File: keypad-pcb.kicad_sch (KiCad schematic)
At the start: 34 parts, among them J1 AVR-ISP-6, SW0 SW_Push, SW1 SW_Push, SW2 SW_Push, SW3 SW_Push, SW4 SW_Push, SW5 SW_Push, SW6 SW_Push, U1 ATmega32U4-A, Y1 Crystal_GND24_Small

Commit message: arrange parts
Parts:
- removed R5, R6: 22, Resistor_SMD:R_0805_2012Metric, symbol Device:R_Small
- F1: value Polyfuse_Small -> 500m
- SW0: value SW_Push -> RESET
- Y1: value Crystal_GND24_Small -> XTAL
- renumbered SW1 to K1, SW2 to K2, SW3 to K3, SW4 to K4, SW5 to K5, SW6 to K6
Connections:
- net D+: now also D1.2 (I/O1), USB1.6 (DP1), USB1.8 (DP2)
- net D-: now also D1.3 (I/O2), USB1.5 (DN2), USB1.7 (DN1)
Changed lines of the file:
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@@
     (stroke (width 0) (type default))
   )
-  (wire (pts (xy 62.23 171.45) (xy 67.31 171.45))
+  (wire (pts (xy 52.07 171.45) (xy 67.31 171.45))
     (stroke (width 0) (type default))
   )
@@
     (stroke (width 0) (type default))
   )
-  (wire (pts (xy 53.34 173.99) (xy 57.15 173.99))
+  (wire (pts (xy 53.34 173.99) (xy 67.31 173.99))
     (stroke (width 0) (type default))
   )
@@
     (stroke (width 0) (type default))
   )
-  (wire (pts (xy 62.23 173.99) (xy 67.31 173.99))
-    (stroke (width 0) (type default))
-  )
   (wire (pts (xy 26.67 39.37) (xy 35.56 39.37))
     (stroke (width 0) (type default))
   )
   (wire (pts (xy 53.34 58.42) (xy 71.12 58.42))
-    (stroke (width 0) (type default))
-  )
-  (wire (pts (xy 52.07 171.45) (xy 57.15 171.45))
     (stroke (width 0) (type default))
   )
@@
   (symbol (lib_id "Switch:SW_Push") (at 40.64 50.8 0) (unit 1)
     (in_bom yes) (on_board yes) (dnp no) (fields_autoplaced)
-    (property "Reference" "SW4" (at 40.64 43.18 0)
+    (property "Reference" "K4" (at 40.64 45.72 0)
       (effects (font (size 1.27 1.27)))
     )
     (property "Value" "SW_Push" (at 40.64 45.72 0)
-      (effects (font (size 1.27 1.27)))
+      (effects (font (size 1.27 1.27)) hide)
     )
     (property "Footprint" "marbastlib-mx:SW_MX_HS_1u" (at 40.64 45.72 0)
@@
       (project "keypad-pcb"
         (path "/73f1bcf6-a3cb-4955-8c73-ee07117345ce"
-          (reference "SW4") (unit 1)
-        )
-      )
-    )
-  )
-  (symbol (lib_id "Device:R_Small") (at 59.69 173.99 90) (unit 1)
-    (in_bom yes) (on_board yes) (dnp no)
-    (property "Reference" "R5" (at 59.69 176.53 90)
-      (effects (font (size 1.27 1.27)))
-    )
-    (property "Value" "22" (at 59.69 179.07 90)
-      (effects (font (size 1.27 1.27)))
-    )
-    (property "Footprint" "Resistor_SMD:R_0805_2012Metric" (at 59.69 173.99 0)
-      (effects (font (size 1.27 1.27)) hide)
-    )
-    (property "Datasheet" "~" (at 59.69 173.99 0)
-      (effects (font (size 1.27 1.27)) hide)
-    )
-    (pin "1")
-    (pin "2")
-    (instances
-      (project "keypad-pcb"
-        (path "/73f1bcf6-a3cb-4955-8c73-ee07117345ce"
-          (reference "R5") (unit 1)
-        )
-      )
-    )
-  )
-  (symbol (lib_id "Device:R_Small") (at 59.69 171.45 90) (unit 1)
-    (in_bom yes) (on_board yes) (dnp no) (fields_autoplaced)
-    (property "Reference" "R6" (at 59.69 166.37 90)
-      (effects (font (size 1.27 1.27)))
-    )
-    (property "Value" "22" (at 59.69 168.91 90)
-      (effects (font (size 1.27 1.27)))
-    )
-    (property "Footprint" "Resistor_SMD:R_0805_2012Metric" (at 59.69 171.45 0)
-      (effects (font (size 1.27 1.27)) hide)
-    )
-    (property "Datasheet" "~" (at 59.69 171.45 0)
-      (effects (font (size 1.27 1.27)) hide)
-    )
-    (pin "1")
-    (pin "2")
-    (instances
-      (project "keypad-pcb"
-        (path "/73f1bcf6-a3cb-4955-8c73-ee07117345ce"
-          (reference "R6") (unit 1)
+          (reference "K4") (unit 1)
         )
       )
@@
   (symbol (lib_id "Switch:SW_Push") (at 58.42 31.75 0) (unit 1)
     (in_bom yes) (on_board yes) (dnp no) (fields_autoplaced)
-    (property "Reference" "SW2" (at 58.42 24.13 0)
+    (property "Reference" "K2" (at 58.42 26.67 0)
       (effects (font (size 1.27 1.27)))
     )
     (property "Value" "SW_Push" (at 58.42 26.67 0)
-      (effects (font (size 1.27 1.27)))
+      (effects (font (size 1.27 1.27)) hide)
     )
     (property "Footprint" "marbastlib-mx:SW_MX_HS_1u" (at 58.42 26.67 0)
@@
       (project "keypad-pcb"
         (path "/73f1bcf6-a3cb-4955-8c73-ee07117345ce"
-          (reference "SW2") (unit 1)
+          (reference "K2") (unit 1)
         )
       )
@@
   (symbol (lib_id "Switch:SW_Push") (at 40.64 31.75 0) (unit 1)
     (in_bom yes) (on_board yes) (dnp no) (fields_autoplaced)
-    (property "Reference" "SW1" (at 40.64 24.13 0)
+    (property "Reference" "K1" (at 40.64 26.67 0)
       (effects (font (size 1.27 1.27)))
     )
     (property "Value" "SW_Push" (at 40.64 26.67 0)
-      (effects (font (size 1.27 1.27)))
+      (effects (font (size 1.27 1.27)) hide)
     )
     (property "Footprint" "marbastlib-mx:SW_MX_HS_1u" (at 40.64 26.67 0)
@@
       (project "keypad-pcb"
         (path "/73f1bcf6-a3cb-4955-8c73-ee07117345ce"
-          (reference "SW1") (unit 1)
+          (reference "K1") (unit 1)
         )
       )
@@
       (effects (font (size 1.27 1.27)))
     )
-    (property "Value" "Polyfuse_Small" (at 66.04 154.94 90)
+    (property "Value" "500m" (at 66.04 154.94 90)
       (effects (font (size 1.27 1.27)))
     )
@@
   (symbol (lib_id "Switch:SW_Push") (at 58.42 50.8 0) (unit 1)
     (in_bom yes) (on_board yes) (dnp no) (fields_autoplaced)
-    (property "Reference" "SW5" (at 58.42 43.18 0)
+    (property "Reference" "K5" (at 58.42 45.72 0)
       (effects (font (size 1.27 1.27)))
     )
     (property "Value" "SW_Push" (at 58.42 45.72 0)
-      (effects (font (size 1.27 1.27)))
+      (effects (font (size 1.27 1.27)) hide)
     )
     (property "Footprint" "marbastlib-mx:SW_MX_HS_1u" (at 58.42 45.72 0)
@@
       (project "keypad-pcb"
         (path "/73f1bcf6-a3cb-4955-8c73-ee07117345ce"
-          (reference "SW5") (unit 1)
+          (reference "K5") (unit 1)
         )
       )
@@
   (symbol (lib_id "Switch:SW_Push") (at 76.2 50.8 0) (unit 1)
     (in_bom yes) (on_board yes) (dnp no) (fields_autoplaced)
-    (property "Reference" "SW6" (at 76.2 43.18 0)
+    (property "Reference" "K6" (at 76.2 45.72 0)
       (effects (font (size 1.27 1.27)))
     )
     (property "Value" "SW_Push" (at 76.2 45.72 0)
-      (effects (font (size 1.27 1.27)))
+      (effects (font (size 1.27 1.27)) hide)
     )
     (property "Footprint" "marbastlib-mx:SW_MX_HS_1u" (at 76.2 45.72 0)
@@
       (project "keypad-pcb"
         (path "/73f1bcf6-a3cb-4955-8c73-ee07117345ce"
-          (reference "SW6") (unit 1)
+          (reference "K6") (unit 1)
         )
       )
@@
       (effects (font (size 1.27 1.27)))
     )
-    (property "Value" "SW_Push" (at 191.77 135.89 0)
+    (property "Value" "RESET" (at 191.77 135.89 0)
       (effects (font (size 1.27 1.27)))
     )
@@
       (effects (font (size 1.27 1.27)))
     )
-    (property "Value" "Crystal_GND24_Small" (at 229.87 62.23 0)
+    (property "Value" "XTAL" (at 229.87 62.23 0)
       (effects (font (size 1.27 1.27)))
     )
@@
   (symbol (lib_id "Switch:SW_Push") (at 76.2 31.75 0) (unit 1)
     (in_bom yes) (on_board yes) (dnp no) (fields_autoplaced)
-    (property "Reference" "SW3" (at 76.2 24.13 0)
+    (property "Reference" "K3" (at 76.2 26.67 0)
       (effects (font (size 1.27 1.27)))
     )
     (property "Value" "SW_Push" (at 76.2 26.67 0)
-      (effects (font (size 1.27 1.27)))
+      (effects (font (size 1.27 1.27)) hide)
     )
     (property "Footprint" "marbastlib-mx:SW_MX_HS_1u" (at 76.2 26.67 0)
@@
       (project "keypad-pcb"
         (path "/73f1bcf6-a3cb-4955-8c73-ee07117345ce"
-          (reference "SW3") (unit 1)
-        )
-      )
+          (reference "K3") (unit 1)
+        )
+      )

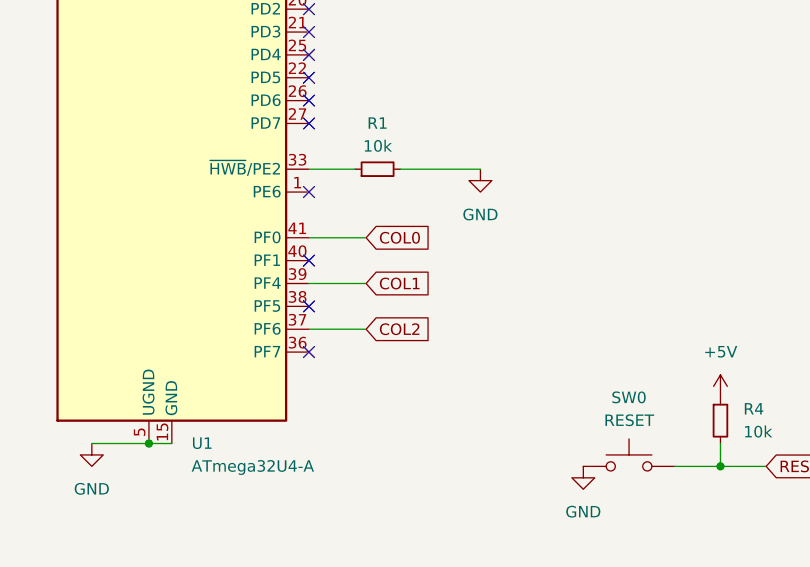
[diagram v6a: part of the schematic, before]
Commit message: complete routing
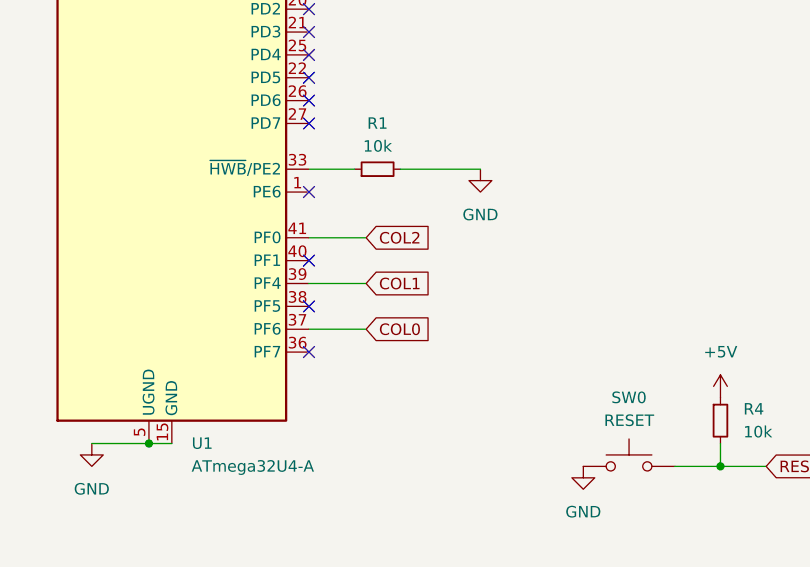
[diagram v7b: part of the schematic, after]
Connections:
- net COL0: now also U1.37 (PF6); no longer U1.41 (PF0)
- net COL2: now also U1.41 (PF0); no longer U1.37 (PF6)
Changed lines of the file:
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@@
     )
   )
-  (global_label "COL2" (shape input) (at 162.56 125.73 0) (fields_autoplaced)
+  (global_label "COL2" (shape input) (at 162.56 115.57 0) (fields_autoplaced)
     (effects (font (size 1.27 1.27)) (justify left))
-    (property "Intersheetrefs" "${INTERSHEET_REFS}" (at 170.3833 125.73 0)
+    (property "Intersheetrefs" "${INTERSHEET_REFS}" (at 170.3833 115.57 0)
       (effects (font (size 1.27 1.27)) (justify left) hide)
     )
@@
     )
   )
-  (global_label "COL0" (shape input) (at 162.56 115.57 0) (fields_autoplaced)
+  (global_label "COL0" (shape input) (at 162.56 125.73 0) (fields_autoplaced)
     (effects (font (size 1.27 1.27)) (justify left))
-    (property "Intersheetrefs" "${INTERSHEET_REFS}" (at 170.3833 115.57 0)
+    (property "Intersheetrefs" "${INTERSHEET_REFS}" (at 170.3833 125.73 0)
       (effects (font (size 1.27 1.27)) (justify left) hide)
     )
